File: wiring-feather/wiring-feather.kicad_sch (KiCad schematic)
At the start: 16 parts, among them J1 M Battery 1, J2 M Battery 1, J3 Screw_Terminal_01x02, J4 Screw_Terminal_01x02, J5 JST Breakout Board, J6 JST Breakout Board, J7 Screw_Terminal_01x02, J8 Screw_Terminal_01x02, M1 Micromotor, M2 Micromotor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

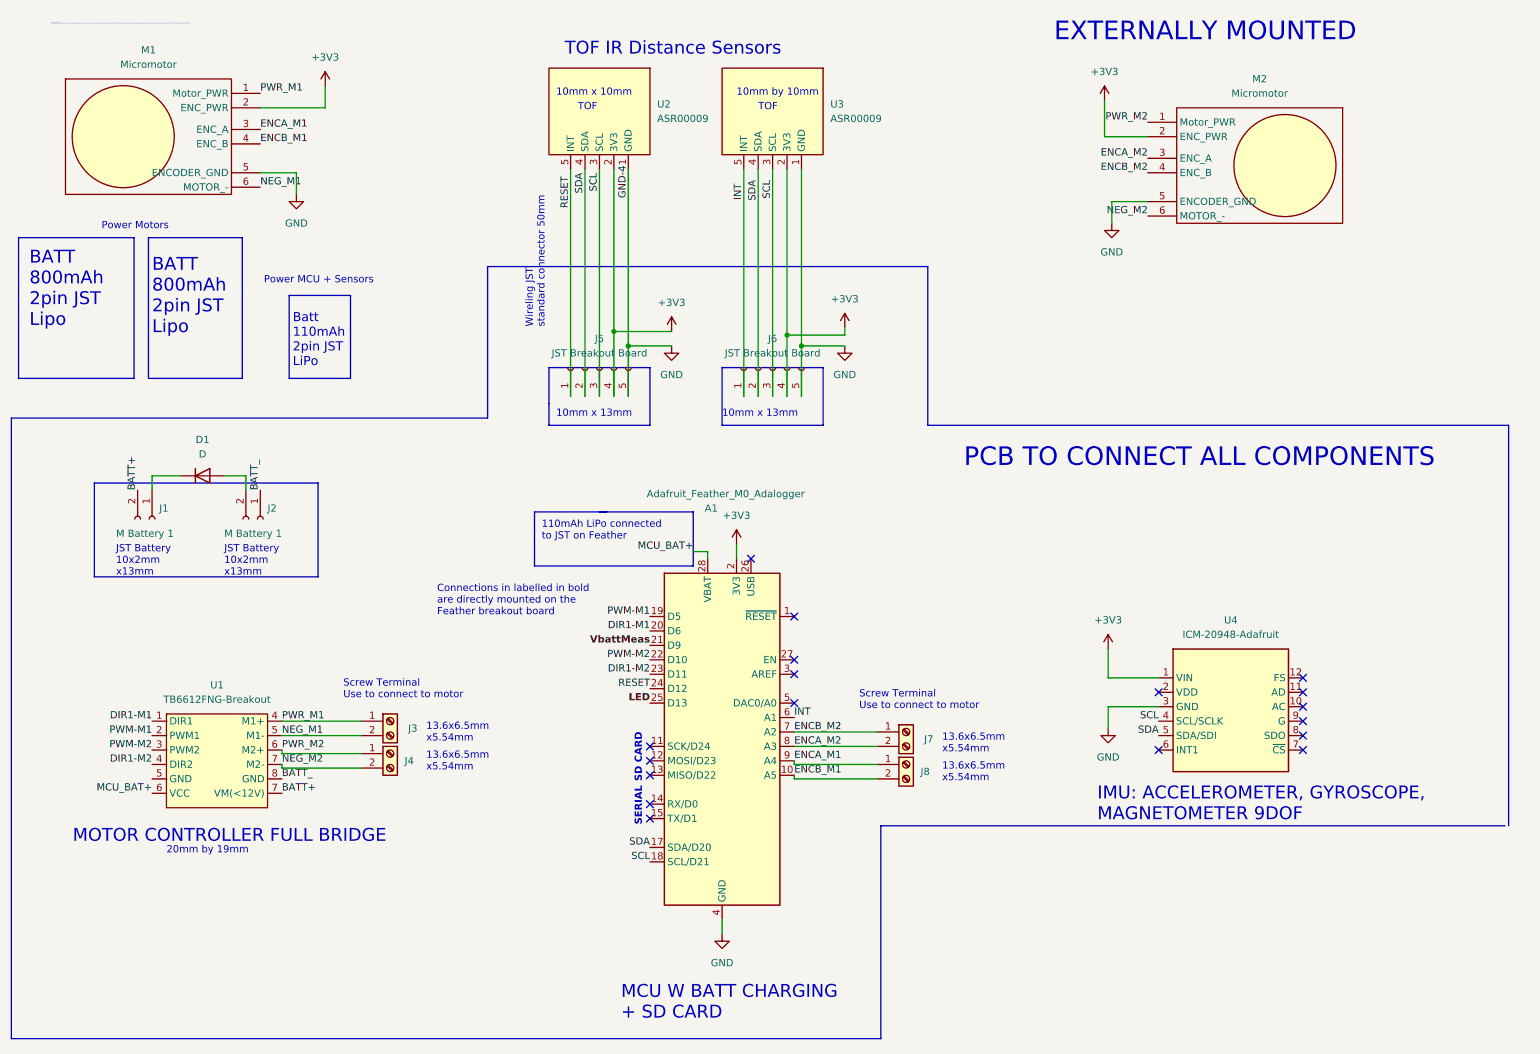
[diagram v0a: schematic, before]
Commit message: Some small changes footprint library
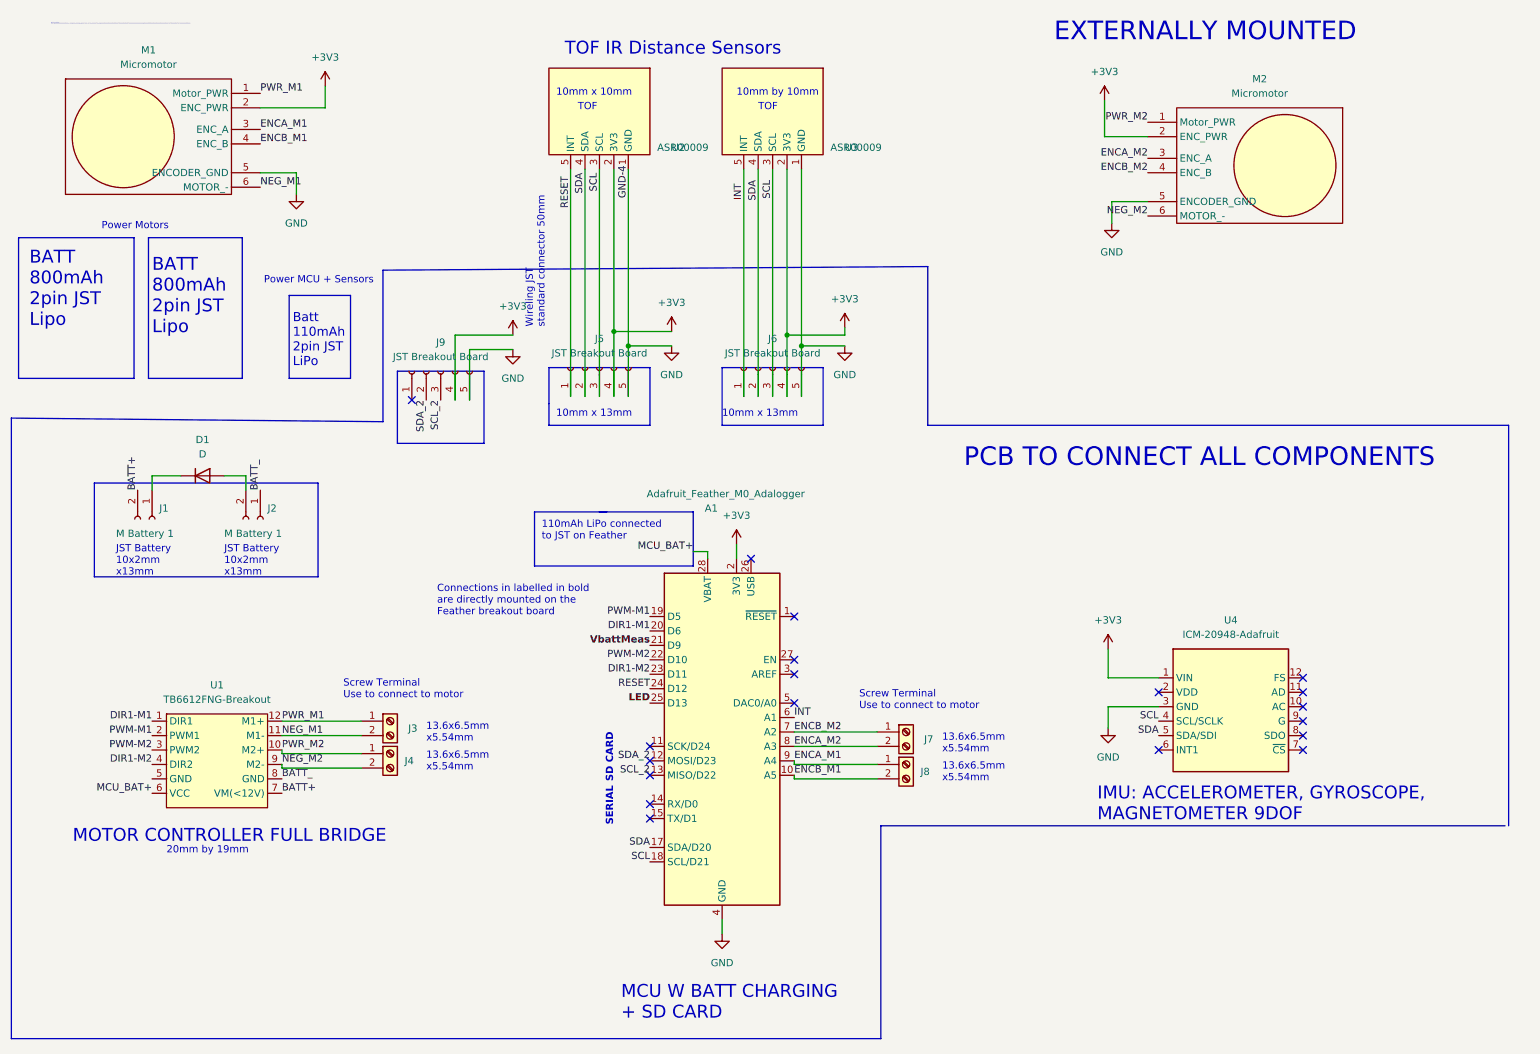
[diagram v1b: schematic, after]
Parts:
- added J9: JST Breakout Board, symbol Connector:Conn_01x05_Female
- U2, U3: Breakout datasheet (none) -> https://media.digikey.com/pdf/Data%20Sheets/TinyCircuits%20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; breakout  (none) -> https://tinycircuits.com/products/tof-distance-sensor-wirel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
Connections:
- net +3V3: now also J9.4 (Pin_4)
- net GND: now also J9.5 (Pin_5)
- net NEG_M1: now also U1.11 (M1-); no longer U1.5 (M1-)
- net NEG_M2: now also U1.9 (M2-); no longer U1.7 (VM(<12V))
- net PWR_M1: now also U1.12 (M1+); no longer U1.4 (M1+)
- net PWR_M2: now also U1.10 (M2+); no longer U1.6 (VCC)
- net SDA_2: now reaches A1.12 (MOSI/D23)
- net SDA_2: now also J9.2 (Pin_2)
- net SCL_2: now reaches A1.13 (MISO/D22)
- net SCL_2: now also J9.3 (Pin_3)
- no-connect marks 18 -> 19

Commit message: Created footprint for components
All components have footprints, approx for the IMU, auto placed them on the PCB
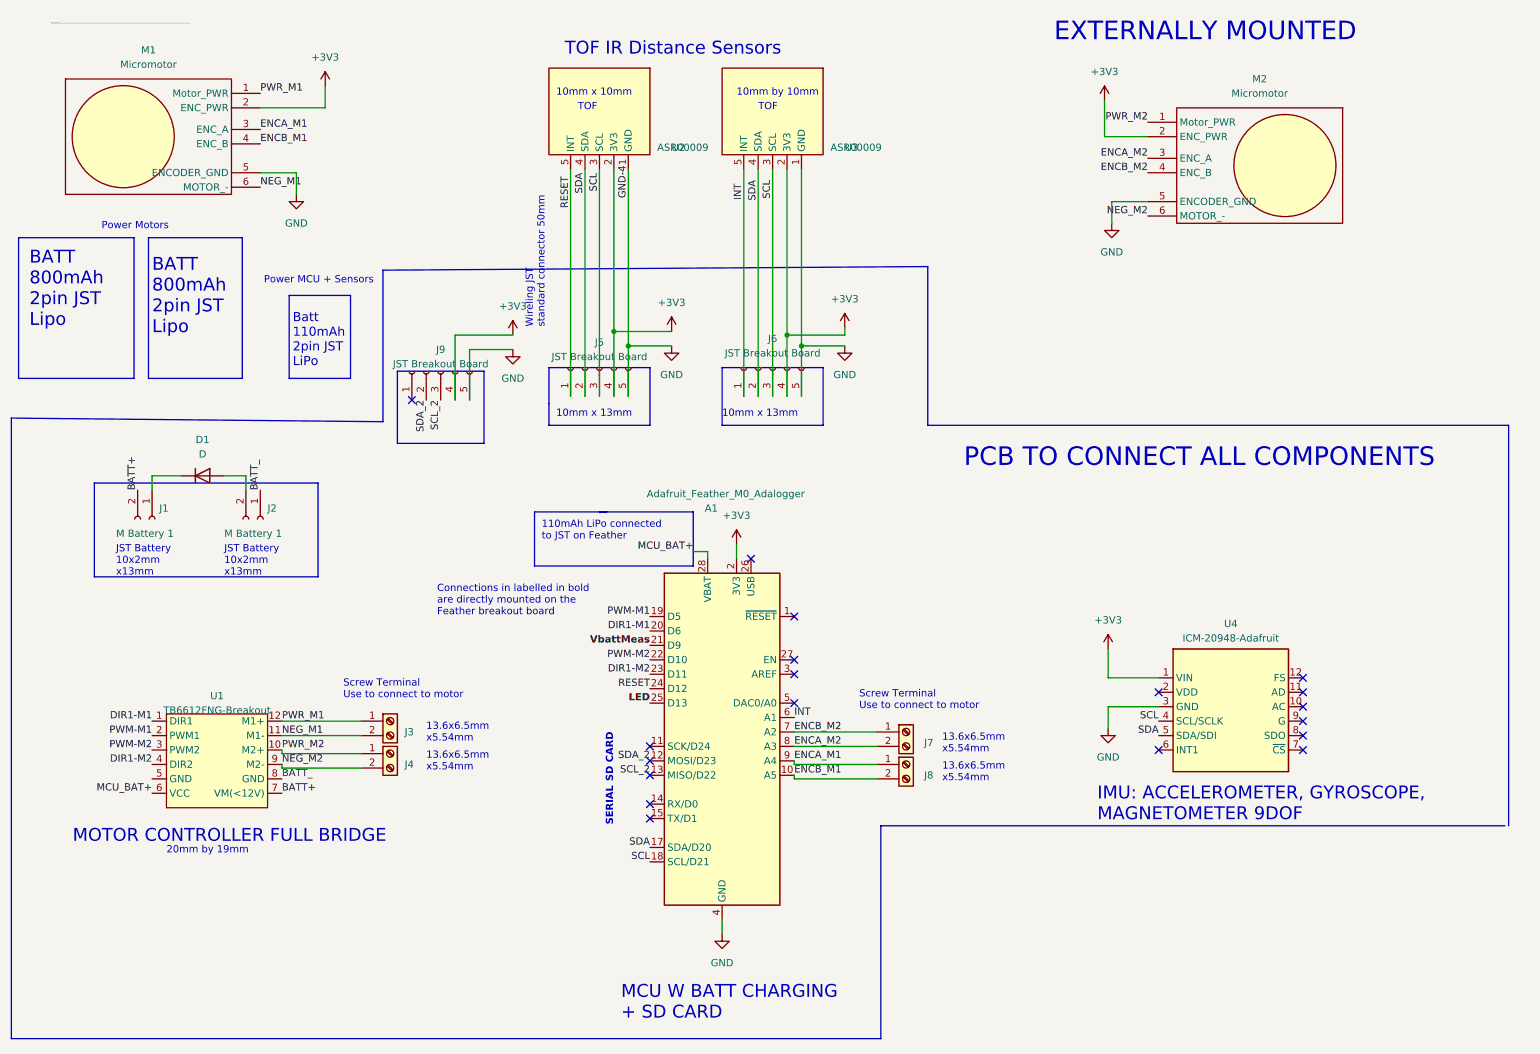
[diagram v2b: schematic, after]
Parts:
- A1: footprint Module:Adafruit_Feather -> 380_footprint-lib:Adafruit_Feather_M0_Adalogger
- J1, J2, J5, J6, J9: footprint (none) -> 380_footprint-lib:JST_breakout
- J3, J4, J7, J8: footprint (none) -> 380_footprint-lib:Screw_terminal_TE_Connectivity
- U1: footprint (none) -> 380_footprint-lib:DRI0044
- U4: footprint Sensor_Motion:InvenSense_QFN-24_3x3mm_P0.4mm -> 380_footprint-lib:ICM-20948

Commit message: made rough pcb
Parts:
- D1: footprint (none) -> Connector_PinHeader_2.54mm:PinHeader_1x02_P2.54mm_Vertical
- J1, J2: footprint 380_footprint-lib:JST_breakout -> Connector_JST:JST_XH_S2B-XH-A_1x02_P2.50mm_Horizontal
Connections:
- net BATT+: now also J1.1 (Pin_1); no longer J1.2 (Pin_2)
- net BATT_: now also J2.2 (Pin_2); no longer J2.1 (Pin_1)
- net DIR1-M1: now also A1.24 (D12); no longer A1.20 (D6)
- net DIR1-M2: now also A1.20 (D6); no longer A1.23 (D11)
- net GND: now also U1.5 (GND)
- net PWM-M1: now also A1.23 (D11); no longer A1.19 (D5)
- net RESET: now also A1.19 (D5); no longer A1.24 (D12)
- net at D1.1 (K): now also J1.2 (Pin_2); no longer J1.1 (Pin_1)
- net at D1.2 (A): now also J2.1 (Pin_1); no longer J2.2 (Pin_2)
- no-connect marks 19 -> 17
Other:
- moved on the sheet: D1, J1, J2, J3, J5, J6, J7, J8, M1, M2, U1, U4

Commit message: updated pcb
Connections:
- net NEG_M2: now also J4.1 (Pin_1); no longer J4.2 (Pin_2)
- net PWR_M2: now also J4.2 (Pin_2); no longer J4.1 (Pin_1)
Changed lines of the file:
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@@
     )
   )
-  (symbol (lib_id "Connector:Screw_Terminal_01x02") (at 86.36 144.78 0) (unit 1)
-    (in_bom yes) (on_board yes) (dnp no) (fields_autoplaced)
-    (property "Reference" "J4" (at 88.9 146.685 0)
+  (symbol (lib_id "Connector:Screw_Terminal_01x02") (at 86.36 147.32 0) (mirror x) (unit 1)
+    (in_bom yes) (on_board yes) (dnp no)
+    (property "Reference" "J4" (at 88.9 145.415 0)
       (effects (font (size 1.27 1.27)) (justify left))
     )
-    (property "Value" "Screw_Terminal_01x02" (at 85.0901 149.86 90)
+    (property "Value" "Screw_Terminal_01x02" (at 85.0901 142.24 90)
       (effects (font (size 1.27 1.27)) (justify right) hide)
     )
-    (property "Footprint" "380_footprint-lib:Screw_terminal_TE_Connectivity" (at 86.36 144.78 0)
+    (property "Footprint" "380_footprint-lib:Screw_terminal_TE_Connectivity" (at 86.36 147.32 0)
       (effects (font (size 1.27 1.27)) hide)
     )
-    (property "Datasheet" "~" (at 86.36 144.78 0)
+    (property "Datasheet" "~" (at 86.36 147.32 0)
       (effects (font (size 1.27 1.27)) hide)
     )

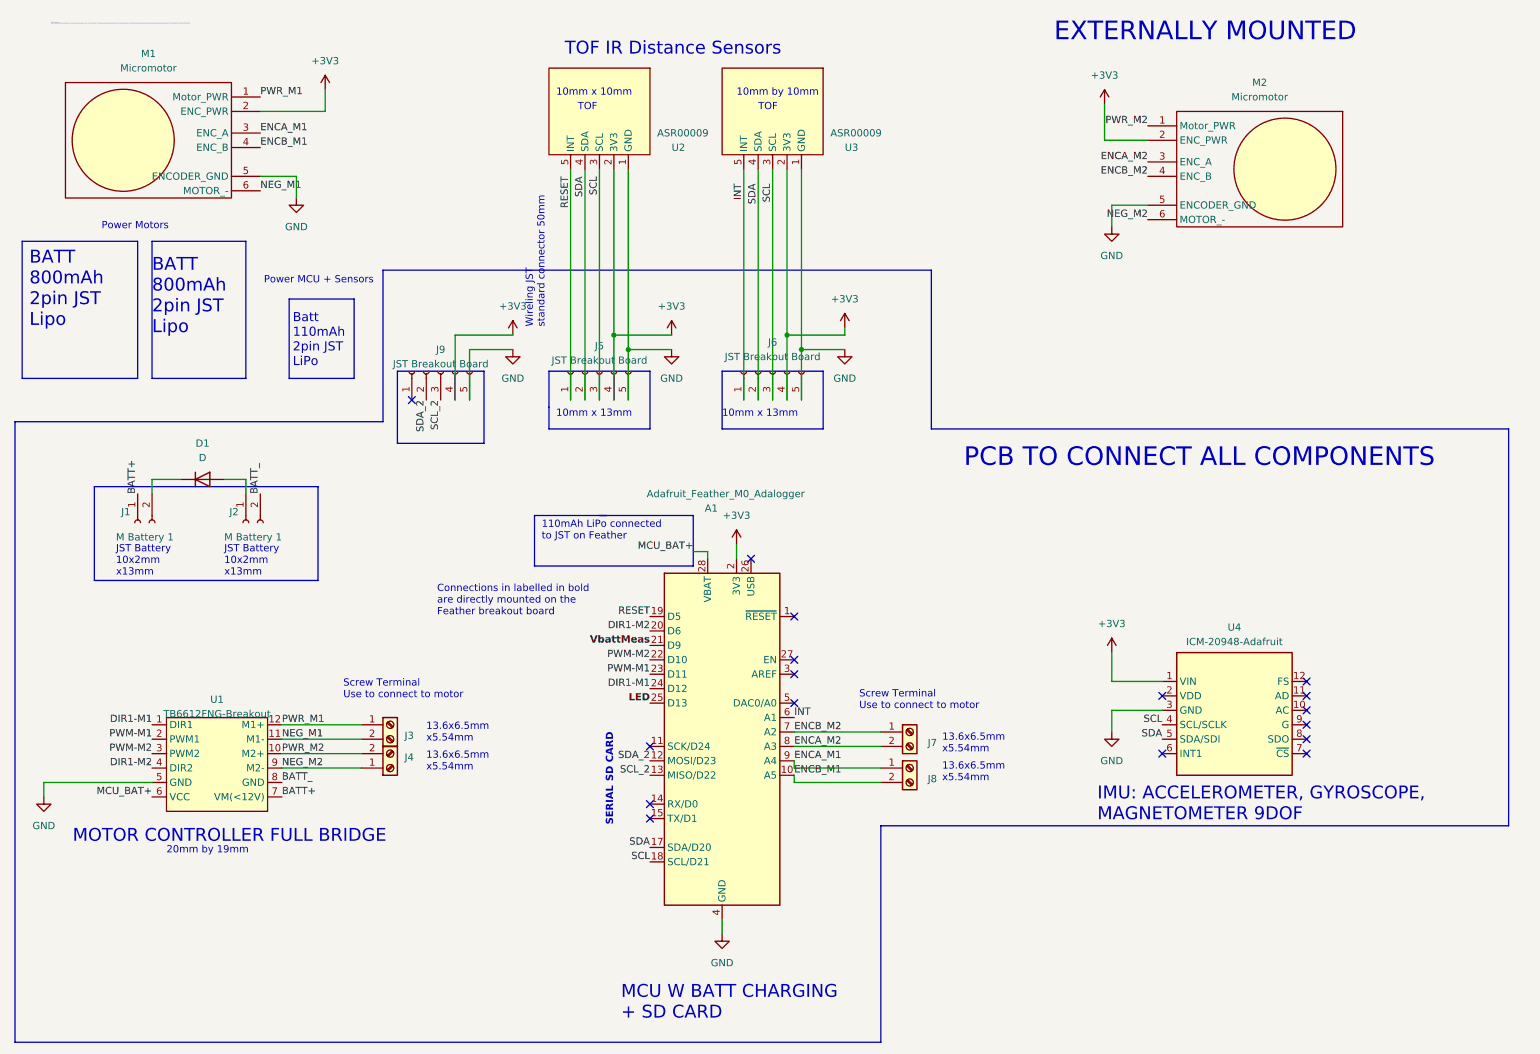
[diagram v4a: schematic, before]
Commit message: Added testing points, i2c pullup resistors
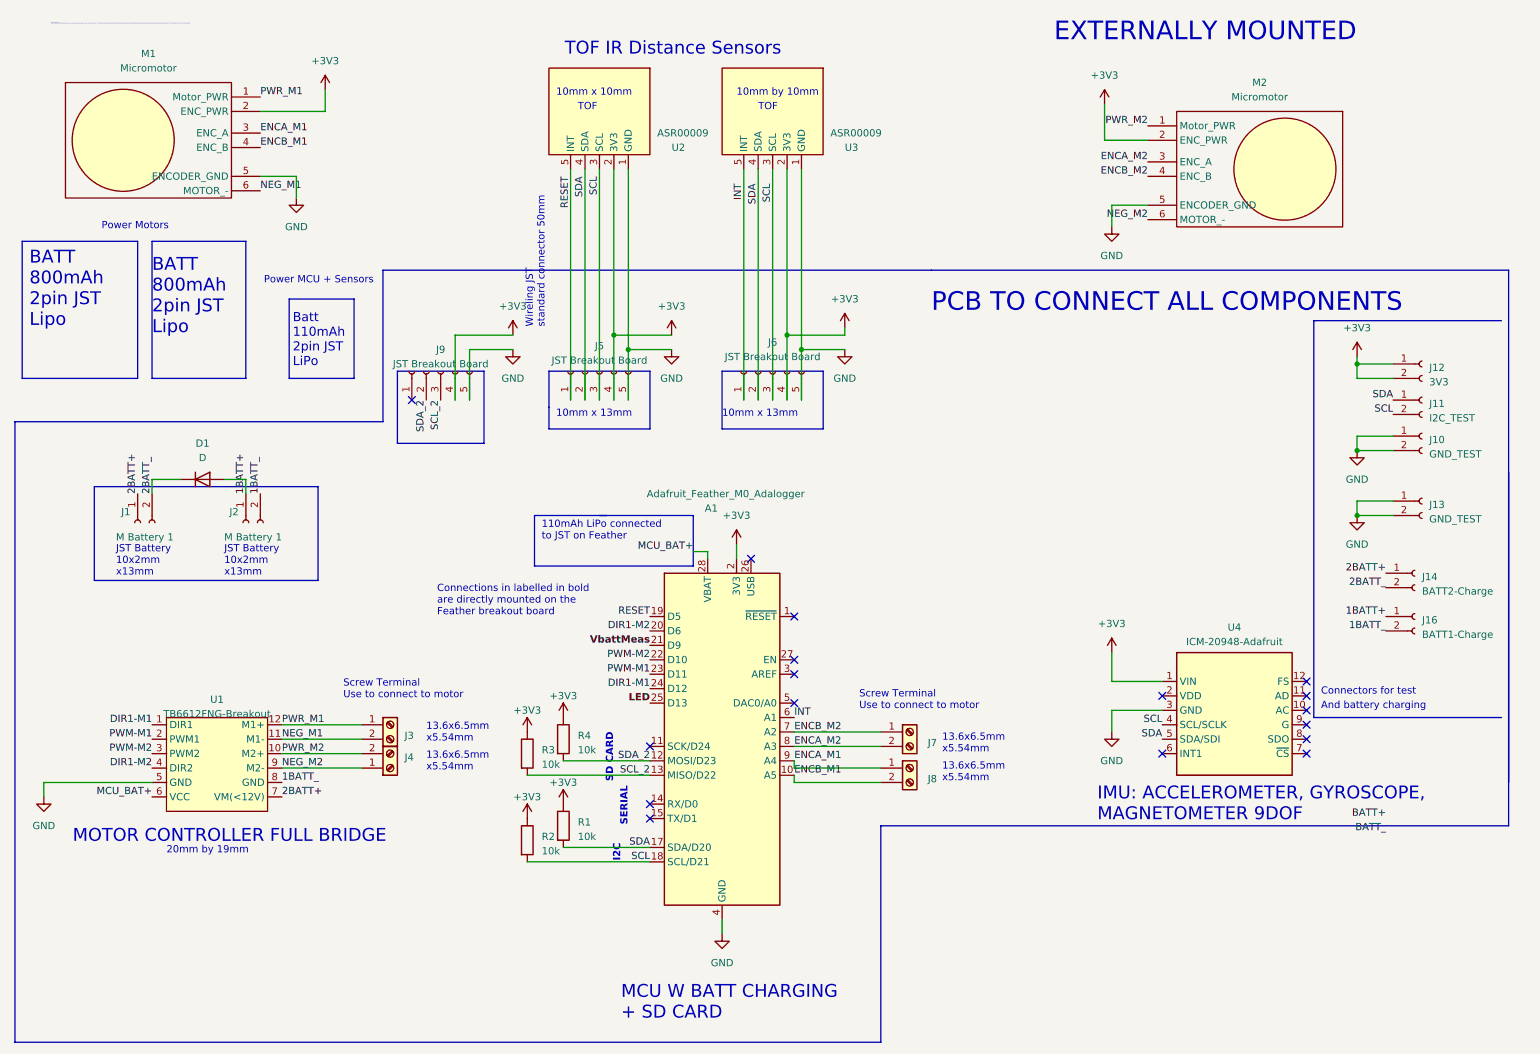
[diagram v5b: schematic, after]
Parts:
- added J10, J13: GND_TEST, Connector_PinSocket_2.54mm:PinSocket_1x02_P2.54mm_Vertical, symbol Connector:Conn_01x02_Socket
- added J11: I2C_TEST, Connector_PinSocket_2.54mm:PinSocket_1x02_P2.54mm_Vertical, symbol Connector:Conn_01x02_Socket
- added J12: 3V3, Connector_PinSocket_2.54mm:PinSocket_1x02_P2.54mm_Vertical, symbol Connector:Conn_01x02_Socket
- added J14: BATT2-Charge, Connector_PinSocket_2.54mm:PinSocket_1x02_P2.54mm_Vertical, symbol Connector:Conn_01x02_Socket
- added J16: BATT1-Charge, Connector_PinSocket_2.54mm:PinSocket_1x02_P2.54mm_Vertical, symbol Connector:Conn_01x02_Socket
- added R1, R2, R3, R4: 10k, Resistor_SMD:R_0805_2012Metric_Pad1.20x1.40mm_HandSolder, symbol Device:R
- J1, J2: footprint Connector_JST:JST_XH_S2B-XH-A_1x02_P2.50mm_Horizontal -> Connector_JST:JST_PH_S2B-PH-K_1x02_P2.00mm_Horizontal; symbol Connector:Conn_01x02_Female -> Connector:Conn_01x02_Socket
- J5, J6, J9: symbol Connector:Conn_01x05_Female -> Connector:Conn_01x05_Socket
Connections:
- net +3V3: now also J12.1 (Pin_1), J12.2 (Pin_2), R1.1, R2.1, R3.1, R4.1
- net BATT+: no longer J1.1 (Pin_1), U1.7 (VM(<12V))
- net BATT_: no longer J2.2 (Pin_2), U1.8 (GND)
- net GND: now also J10.1 (Pin_1), J10.2 (Pin_2), J13.1 (Pin_1), J13.2 (Pin_2)
- net SCL: now also J11.2 (Pin_2), R2.2
- net SCL_2: now also R3.2
- net SDA: now also J11.1 (Pin_1), R1.2
- net SDA_2: now also R4.2
- net 2BATT_: now reaches D1.1 (K), J1.2 (Pin_2)
- net 2BATT_: now also J14.2 (Pin_2)
- net 1BATT+: now reaches D1.2 (A), J2.1 (Pin_1)
- net 1BATT+: now also J16.1 (Pin_1)
- new net 1BATT_: J16.2 (Pin_2), J2.2 (Pin_2), U1.8 (GND)
- new net 2BATT+: J1.1 (Pin_1), J14.1 (Pin_1), U1.7 (VM(<12V))
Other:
- note added: "And battery charging"
- note added: "Connectors for test"
- note added: "I2C"
